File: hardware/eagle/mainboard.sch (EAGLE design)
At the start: 31 parts, among them Q101 16MHz

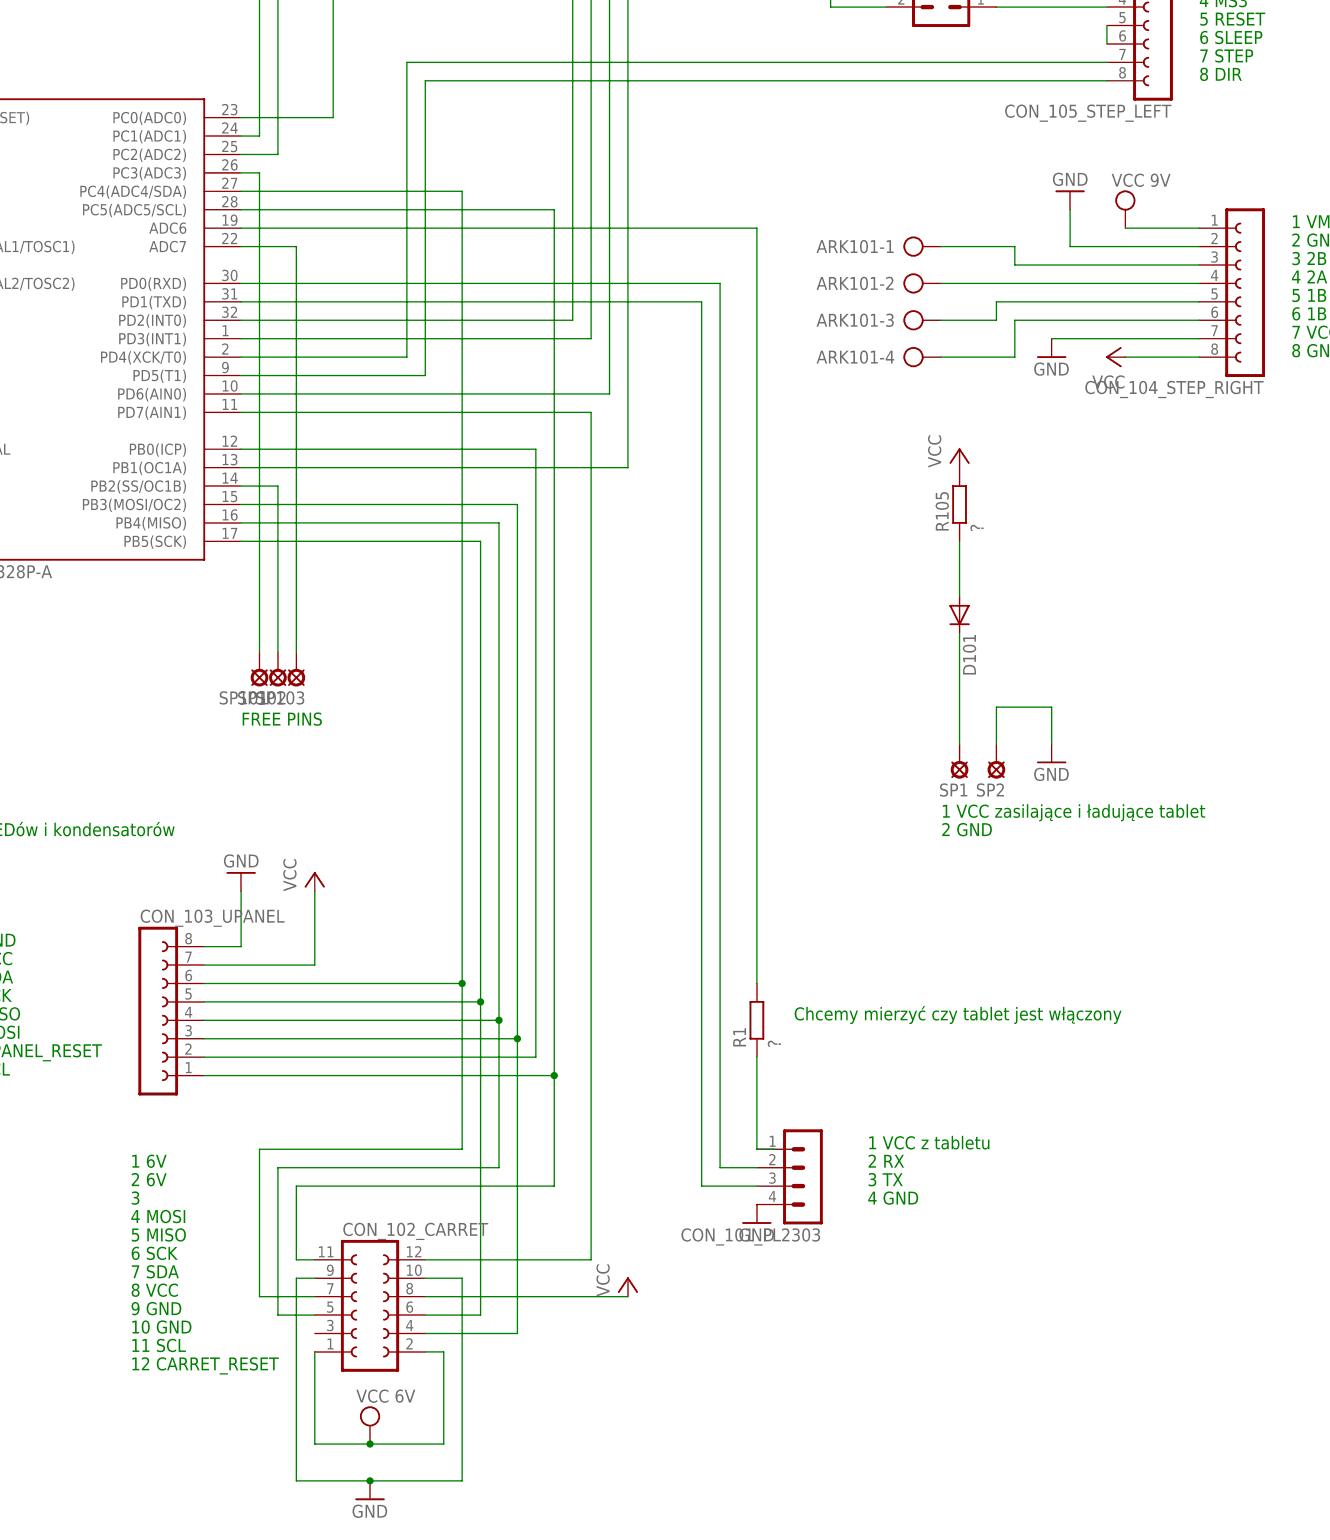
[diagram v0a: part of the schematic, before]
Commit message: 
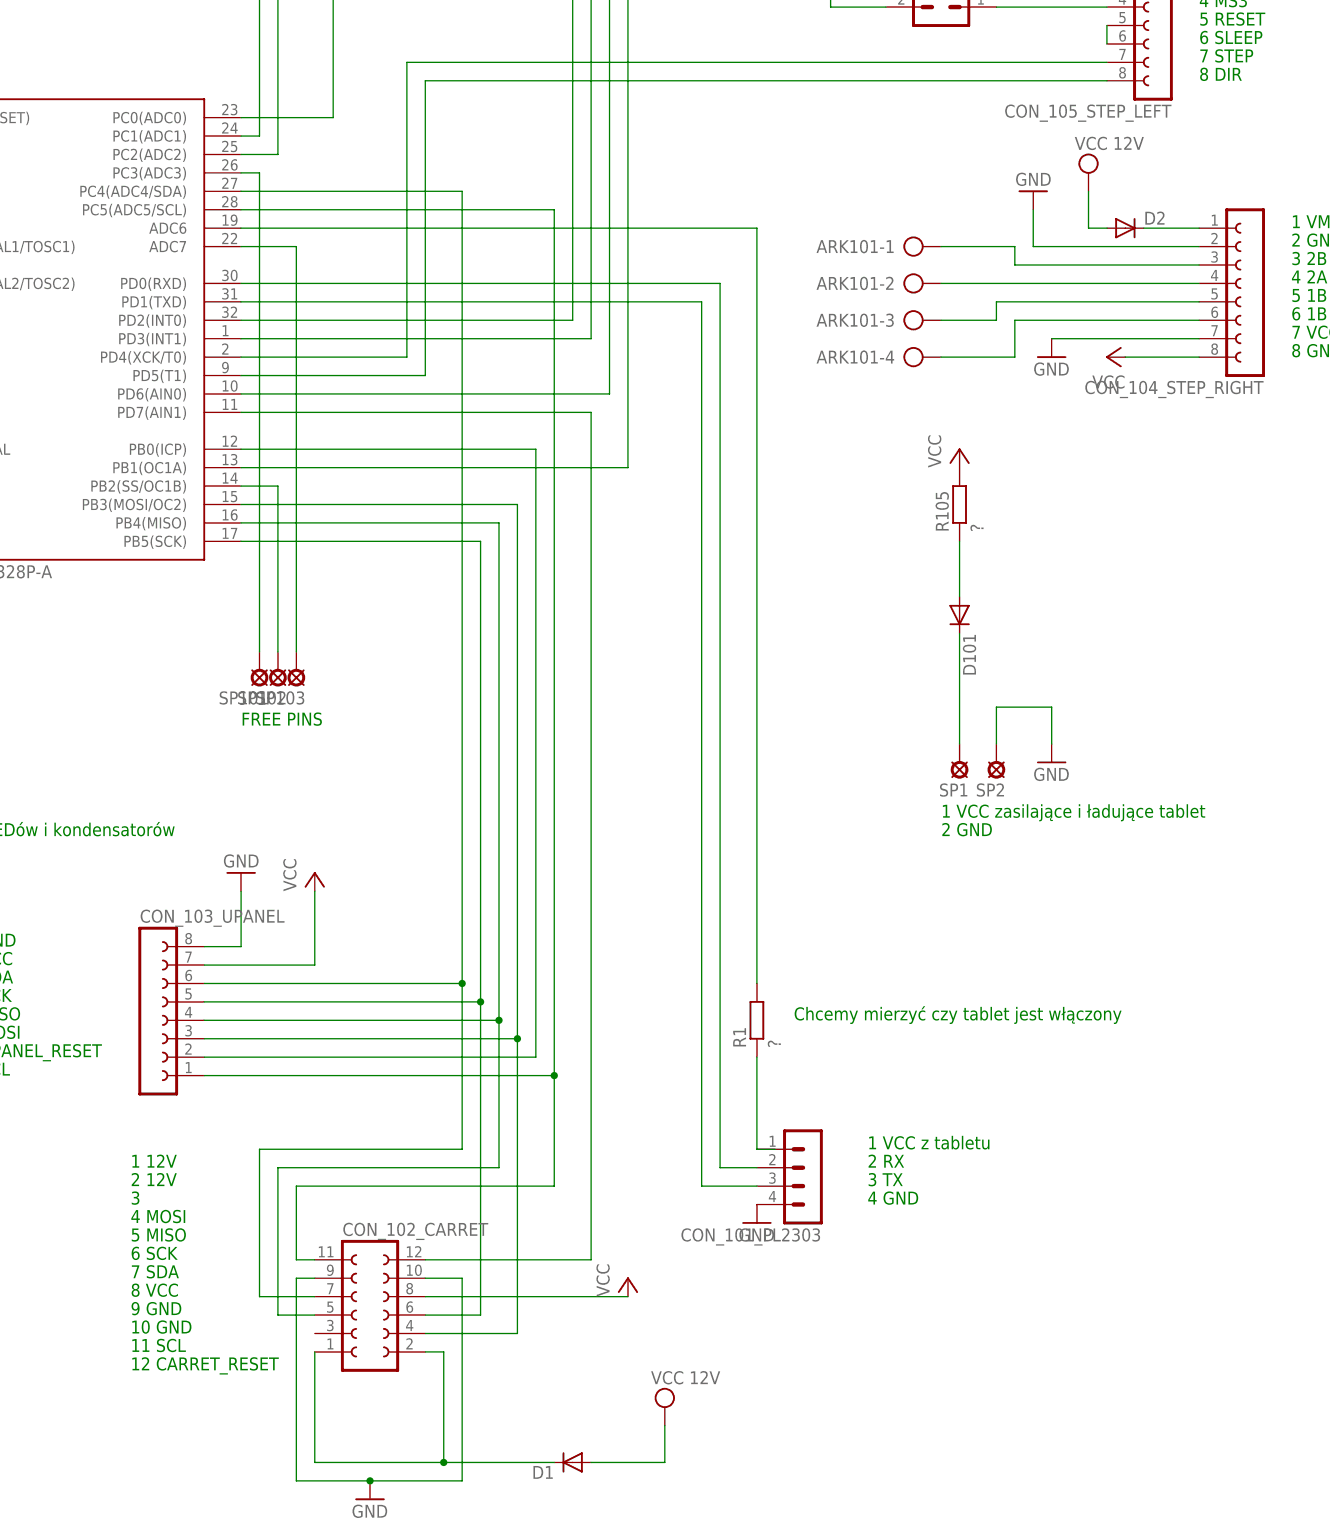
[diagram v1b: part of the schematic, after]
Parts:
- added D1, D2: 1N5060GP, diode:1N5060GP
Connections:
- new net N$22: CON_104_STEP_RIGHT.1, D2.C
- new net N$23: CON_102_CARRET.1, CON_102_CARRET.2, D1.C
- net VCC: now also D1.A, D2.A; no longer CON_102_CARRET.1, CON_102_CARRET.2, CON_104_STEP_RIGHT.1
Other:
- note added: "1 12V"
- note added: "2 12V"
- note removed: "1 6V"
- note removed: "2 6V"
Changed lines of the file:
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@@
 <part name="CON_104_STEP_RIGHT" library="con-lsta" deviceset="FE08-1" device=""/>
 <part name="CON_105_STEP_LEFT" library="con-lsta" deviceset="FE08-1" device=""/>
-<part name="SUPPLY1" library="supply2" deviceset="VCC" device="" value="VCC 9V"/>
+<part name="SUPPLY1" library="supply2" deviceset="VCC" device="" value="VCC 12V"/>
 <part name="GND4" library="supply1" deviceset="GND" device=""/>
 <part name="GND5" library="supply1" deviceset="GND" device=""/>
@@
 <part name="GND8" library="supply1" deviceset="GND" device=""/>
 <part name="CON_102_CARRET" library="con-lsta" deviceset="FE06-2" device=""/>
-<part name="SUPPLY2" library="supply2" deviceset="VCC" device="" value="VCC 6V"/>
+<part name="SUPPLY2" library="supply2" deviceset="VCC" device="" value="VCC 12V"/>
 <part name="ARK101" library="con-ptr500" deviceset="AK300/4" device=""/>
 <part name="JUMPER_101" library="con-lstb" deviceset="MA03-2" device=""/>
@@
 <part name="GND9" library="supply1" deviceset="GND" device=""/>
 <part name="R1" library="resistor" deviceset="R-EU_" device="0613/15" value="?"/>
+<part name="D2" library="diode" deviceset="1N5060GP" device="" value=""/>
+<part name="D1" library="diode" deviceset="1N5060GP" device="" value=""/>
 </parts>
 <sheets>
@@
 <text x="-53.34" y="-50.8" size="1.778" layer="91">7 VCC</text>
 <text x="-53.34" y="-48.26" size="1.778" layer="91">8 GND</text>
-<text x="-30.48" y="-78.74" size="1.778" layer="91">1 6V</text>
-<text x="-30.48" y="-81.28" size="1.778" layer="91">2 6V</text>
+<text x="-30.48" y="-78.74" size="1.778" layer="91">1 12V</text>
+<text x="-30.48" y="-81.28" size="1.778" layer="91">2 12V</text>
 <text x="-30.48" y="-83.82" size="1.778" layer="91">3 </text>
 <text x="-30.48" y="-86.36" size="1.778" layer="91">4 MOSI</text>
@@
 <instance part="CON_104_STEP_RIGHT" gate="G$1" x="124.46" y="43.18" rot="R180"/>
 <instance part="CON_105_STEP_LEFT" gate="G$1" x="111.76" y="81.28" rot="R180"/>
-<instance part="SUPPLY1" gate="G$1" x="106.68" y="53.34"/>
-<instance part="GND4" gate="1" x="99.06" y="55.88" rot="R180"/>
+<instance part="SUPPLY1" gate="G$1" x="101.6" y="58.42"/>
+<instance part="GND4" gate="1" x="93.98" y="55.88" rot="R180"/>
 <instance part="GND5" gate="1" x="96.52" y="33.02"/>
 <instance part="P+3" gate="VCC" x="104.14" y="33.02" rot="R90"/>
@@
 <instance part="GND8" gate="1" x="2.54" y="-124.46"/>
 <instance part="CON_102_CARRET" gate="G$1" x="2.54" y="-99.06"/>
-<instance part="SUPPLY2" gate="G$1" x="2.54" y="-114.3"/>
+<instance part="SUPPLY2" gate="G$1" x="43.18" y="-111.76"/>
 <instance part="ARK101" gate="-1" x="76.2" y="48.26"/>
 <instance part="ARK101" gate="-2" x="76.2" y="43.18"/>
@@
 <instance part="GND9" gate="1" x="96.52" y="-22.86"/>
 <instance part="R1" gate="G$1" x="55.88" y="-58.42" rot="R90"/>
+<instance part="D2" gate="1" x="106.68" y="50.8"/>
+<instance part="D1" gate="1" x="30.48" y="-119.38" rot="R180"/>
 </instances>
 <busses>
@@
 </segment>
 <segment>
-<wire x1="116.84" y1="48.26" x2="99.06" y2="48.26" width="0.1524" layer="91"/>
-<wire x1="99.06" y1="48.26" x2="99.06" y2="53.34" width="0.1524" layer="91"/>
-<pinref part="CON_104_STEP_RIGHT" gate="G$1" pin="2"/>
-<pinref part="GND4" gate="1" pin="GND"/>
-</segment>
-<segment>
 <wire x1="96.52" y1="35.56" x2="116.84" y2="35.56" width="0.1524" layer="91"/>
 <pinref part="GND5" gate="1" pin="GND"/>
@@
 <wire x1="88.9" y1="-15.24" x2="88.9" y2="-20.32" width="0.1524" layer="91"/>
 </segment>
+<segment>
+<pinref part="CON_104_STEP_RIGHT" gate="G$1" pin="2"/>
+<pinref part="GND4" gate="1" pin="GND"/>
+<wire x1="116.84" y1="48.26" x2="93.98" y2="48.26" width="0.1524" layer="91"/>
+<wire x1="93.98" y1="48.26" x2="93.98" y2="53.34" width="0.1524" layer="91"/>
+</segment>
 </net>
 <net name="VCC" class="0">
@@
 <pinref part="P+2" gate="VCC" pin="VCC"/>
 <pinref part="R105" gate="G$1" pin="2"/>
-</segment>
-<segment>
-<wire x1="116.84" y1="50.8" x2="106.68" y2="50.8" width="0.1524" layer="91"/>
-<pinref part="CON_104_STEP_RIGHT" gate="G$1" pin="1"/>
-<pinref part="SUPPLY1" gate="G$1" pin="VCC"/>
 </segment>
 <segment>
@@
 </segment>
 <segment>
-<wire x1="2.54" y1="-116.84" x2="-5.08" y2="-116.84" width="0.1524" layer="91"/>
-<wire x1="-5.08" y1="-116.84" x2="-5.08" y2="-104.14" width="0.1524" layer="91"/>
-<wire x1="2.54" y1="-116.84" x2="12.7" y2="-116.84" width="0.1524" layer="91"/>
-<wire x1="12.7" y1="-116.84" x2="12.7" y2="-104.14" width="0.1524" layer="91"/>
-<wire x1="12.7" y1="-104.14" x2="10.16" y2="-104.14" width="0.1524" layer="91"/>
-<junction x="2.54" y="-116.84"/>
-<pinref part="SUPPLY2" gate="G$1" pin="VCC"/>
-<pinref part="CON_102_CARRET" gate="G$1" pin="1"/>
-<pinref part="CON_102_CARRET" gate="G$1" pin="2"/>
-</segment>
-<segment>
 <wire x1="73.66" y1="81.28" x2="66.04" y2="81.28" width="0.1524" layer="91"/>
 <wire x1="66.04" y1="83.82" x2="73.66" y2="83.82" width="0.1524" layer="91"/>
@@
 <pinref part="CON_106_ULTRASOUND" gate="1" pin="1"/>
 </segment>
+<segment>
+<pinref part="D2" gate="1" pin="A"/>
+<pinref part="SUPPLY1" gate="G$1" pin="VCC"/>
+<wire x1="104.14" y1="50.8" x2="101.6" y2="50.8" width="0.1524" layer="91"/>
+<wire x1="101.6" y1="50.8" x2="101.6" y2="55.88" width="0.1524" layer="91"/>
+</segment>
+<segment>
+<pinref part="SUPPLY2" gate="G$1" pin="VCC"/>
+<wire x1="43.18" y1="-114.3" x2="43.18" y2="-119.38" width="0.1524" layer="91"/>
+<pinref part="D1" gate="1" pin="A"/>
+<wire x1="43.18" y1="-119.38" x2="33.02" y2="-119.38" width="0.1524" layer="91"/>
+</segment>
 </net>
 <net name="N$4" class="0">
@@
 </segment>
 </net>
+<net name="N$22" class="0">
+<segment>
+<pinref part="CON_104_STEP_RIGHT" gate="G$1" pin="1"/>
+<pinref part="D2" gate="1" pin="C"/>
+<wire x1="116.84" y1="50.8" x2="109.22" y2="50.8" width="0.1524" layer="91"/>
+</segment>
+</net>
+<net name="N$23" class="0">
+<segment>
+<pinref part="CON_102_CARRET" gate="G$1" pin="2"/>
+<wire x1="12.7" y1="-119.38" x2="12.7" y2="-104.14" width="0.1524" layer="91"/>
+<wire x1="12.7" y1="-104.14" x2="10.16" y2="-104.14" width="0.1524" layer="91"/>
+<pinref part="D1" gate="1" pin="C"/>
+<wire x1="27.94" y1="-119.38" x2="12.7" y2="-119.38" width="0.1524" layer="91"/>
+<wire x1="-5.08" y1="-119.38" x2="-5.08" y2="-104.14" width="0.1524" layer="91"/>
+<pinref part="CON_102_CARRET" gate="G$1" pin="1"/>
+<wire x1="12.7" y1="-119.38" x2="-5.08" y2="-119.38" width="0.1524" layer="91"/>
+<junction x="12.7" y="-119.38"/>
+</segment>
+</net>
